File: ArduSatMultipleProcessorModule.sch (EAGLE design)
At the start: 82 parts, among them IC1 ATMEGA328P, IC2 ATMEGA328P, IC3 ATMEGA328P, IC4 ATMEGA328P, IC5 MCP23017SO, IC6 MCP23017SO, P1 N1_ICSP, P2 N0_ICSP, P3 N0_ICSP, P4 N1_ICSP, Q1 BSS138 N-MOSFET, Q2 BSS138 N-MOSFET, Q3 BSS138 N-MOSFET, Q4 BSS138 N-MOSFET, Q5 BSS138 N-MOSFET, Q6 BSS138 N-MOSFET, Q7 BSS138 N-MOSFET, Q8 BSS138 N-MOSFET, U1 MUX-74HC4067, U2 MUX-74HC4067

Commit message: Testing replacement of latches using ATmega328
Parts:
- added C13, C14: 22pF 0603, freetronics-master-v1.1:CAP0603
- added IC7: ATMEGA328P, freetronics-master-v1.1:AVR-MEGA8-MI
- added P5: N1_ICSP, freetronics-jon:ICSPSMT
- added R26: 22K 0603, freetronics-master-v1.1:RESISTOR0603
- added R32: 1M 0603, freetronics-master-v1.1:RESISTOR0603
- added R33: 33K 0603, freetronics-master-v1.1:RESISTOR0603
- added U$53: CRYSTAL-GND3X2, freetronics-jon:CRYSTAL-GND3X2
- added U3, U4: MUX-74HC4067, SparkFun:MUX-74HC4067SMD
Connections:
- removed net MGMNT_SCL: IC5.SCL, IC6.SCL, R25.1, R27.1
- removed net MGMNT_SDA: IC5.SDA, IC6.SDA, R24.1, R28.1
- removed net S0: IC5.GPA0, U1.S0, U2.S0
- removed net S1: IC5.GPA1, U1.S1, U2.S1
- removed net S2: IC5.GPA2, U1.S2, U2.S2
- removed net S3: IC5.GPA3, U1.S3, U2.S3
- new net N$22: C14.2, IC7.PB7(XTAL2/TOSC2), R32.1, U$53.XTL2
- new net N$23: C13.2, IC7.PB6(XTAL1/TOSC1), R32.2, U$53.XTL1
- new net S_A0: IC5.GPA0, IC7.PC0(ADC0), U1.S0, U2.S0, U3.S0, U4.S0
- new net S_A1: IC5.GPA1, IC7.PC1(ADC1), U1.S1, U2.S1, U3.S1, U4.S1
- new net S_A2: IC5.GPA2, IC7.PC2(ADC2), U1.S2, U2.S2, U3.S2, U4.S2
- new net S_A3: IC5.GPA3, IC7.PC3(ADC3), U1.S3, U2.S3, U3.S3, U4.S3
- new net S_A4_SDA: IC5.SDA, IC6.SDA, IC7.PC4(ADC4/SDA), R24.1, R28.1
- new net S_A5_SCL: IC5.SCL, IC6.SCL, IC7.PC5(ADC5/SCL), R25.1, R27.1
- new net S_A6: IC7.ADC6
- new net S_A7: IC7.ADC7
- new net S_D0_RX: IC7.PD0(RXD)
- new net S_D10: IC7.PB2(SS/OC1B)
- new net S_D11_MOSI: IC7.PB3(MOSI/OC2), P5.4
- new net S_D12_MISO: IC7.PB4(MISO), P5.1
- new net S_D13_SCK: IC7.PB5(SCK), P5.3
- new net S_D1_TX: IC7.PD1(TXD)
- new net S_D2: IC7.PD2(INT0)
- new net S_D3: IC7.PD3(INT1)
- new net S_D4: IC7.PD4(XCK/T0)
- new net S_D5: IC7.PD5(T1)
- new net S_D6: IC7.PD6(AIN0)
- new net S_D7: IC7.PD7(AIN1)
- new net S_D8: IC7.PB0(ICP)
- new net S_D9: IC7.PB1(OC1A)
- new net S_RESET: IC7.PC6(/RESET), P5.5, R26.1
- net +5V_SYS: now also IC7.AREF, IC7.AVCC, IC7.VCC@1, IC7.VCC@2, P5.2, R26.2, U3.VCC, U4.VCC
- net EN: now also R33.2, U3.EN, U4.EN
- net GND: now also C13.1, C14.1, IC7.AGND, IC7.GND@1, IC7.GND@2, P5.6, R33.1, U$53.GND, U$53.GND2, U3.GND, U4.GND
- net N0_D0_RX: now also U4.CHAN0
- net N0_D1_TX: now also U3.CHAN0
- net N10_D0_RX: now also U4.CHAN10
- net N10_D1_TX: now also U3.CHAN10
- net N11_D0_RX: now also U4.CHAN11
- net N11_D1_TX: now also U3.CHAN11
- net N12_D0_RX: now also U4.CHAN12
- net N12_D1_TX: now also U3.CHAN12
- net N13_D0_RX: now also U4.CHAN13
- net N13_D1_TX: now also U3.CHAN13
- net N14_D0_RX: now also U4.CHAN14
- net N14_D1_TX: now also U3.CHAN14
- net N15_D0_RX: now also U4.CHAN15
- net N15_D1_TX: now also U3.CHAN15
- net N1_D0_RX: now also U4.CHAN1
- net N1_D1_TX: now also U3.CHAN1
- net N2_D0_RX: now also U4.CHAN2
- net N2_D1_TX: now also U3.CHAN2
- net N3_D0_RX: now also U4.CHAN3
- net N3_D1_TX: now also U3.CHAN3
- net N4_D0_RX: now also U4.CHAN4
- net N4_D1_TX: now also U3.CHAN4
- net N5_D0_RX: now also U4.CHAN5
- net N5_D1_TX: now also U3.CHAN5
- net N6_D0_RX: now also U4.CHAN6
- net N6_D1_TX: now also U3.CHAN6
- net N7_D0_RX: now also U4.CHAN7
- net N7_D1_TX: now also U3.CHAN7
- net N8_D0_RX: now also U4.CHAN8
- net N8_D1_TX: now also U3.CHAN8
- net N9_D0_RX: now also U4.CHAN9
- net N9_D1_TX: now also U3.CHAN9
- net RX: now also U4.COM
- net TX: now also U3.COM
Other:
- note added: "Supervisor"

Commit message: Added alternative supervisor node
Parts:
- added JP3: (no value), freetronics-master-v1.1:M02PTH
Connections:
- net RX: now also JP3.2
- net TX: now also JP3.1
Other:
- note added: "ATmega328P core consumes ~10mA at 5V / 16MHz"
- note added: "May not be suitable for direct control of node VCCs."
- note removed: "Not suitable for direct control of node VCCs."
- moved on the sheet: C1, C10, C11, C12, C13, C14, C2, C3, C4, C5, C6, C7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

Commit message: Added VCC control for nodes 0 and 1
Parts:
- removed C12: 100nF 0603, freetronics-master-v1.1:CAP0603
- added C15: 100nF 0603, freetronics-master-v1.1:CAP0603
- added Q10, Q9: 2N7002 N-MOSFET, freetronics-master-v1:MOSFET-NCHANNELSMD
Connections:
- net EN renamed UART_EN
- net S_D0_RX renamed S_D0_N2_PWR
- net S_D1_TX renamed S_D1_N3_PWR
- net S_D2 renamed S_D2_N4_PWR
- net S_D3 renamed S_D3_N5_PWR
- net S_D4 renamed S_D4_N6_PWR
- removed net S_A6: IC7.ADC6
- removed net S_A7: IC7.ADC7
- new net S_A6_N0_PWR: IC7.ADC6, Q9.G
- new net S_A7_N1_PWR: IC7.ADC7, Q10.G
- net +5V_SYS: now also Q10.S, Q9.S
- net GND: now also C15.2; no longer C12.2
- net N0_5V: now also Q9.D
- net N1_5V: now also C15.1, Q10.D; no longer C12.1
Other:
- note added: "Add FETs or something to switch node VCCs?"
- note added: "Add watchdog (voltage + heartbeat?) to supervisor"
- note added: "Control UART switch EN from supervisor"
- note added: "Node 0"
- note added: "Node 1"
- note added: "Power Control"
- note added: "Processor"
- note removed: "Add FETs or something to switch node VCCs"
- note removed: "Processor Node 0"
- note removed: "Processor Node 1"
- moved on the sheet: C10, C11, C7, C8, C9, IC3, IC4, P3, P4, Q5, Q6, Q7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

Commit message: Supervisor now has control of both node power and serial comms
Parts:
- removed U1, U2, U3, U4: MUX-74HC4067, SparkFun:MUX-74HC4067SMD
- added IC8: MCP23S17ML, freetronics-jon:MCP23S17ML
- added U$57, U$58, U$59, U$60: MUX-74HC4067-QFNSMT, freetronics-jon:MUX-74HC4067-QFNSMT
- IC5, IC6: value MCP23017SO -> MCP23017ML; device microchip:MCP23017SO -> freetronics-jon:MCP23017ML
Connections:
- net S_D0_N2_PWR renamed S_D0
- net S_D1_N3_PWR renamed S_D1
- net S_D2_N4_PWR renamed S_D2
- net S_D3_N5_PWR renamed S_D3
- net S_D4_N6_PWR renamed S_D4
- removed net N10_5V: IC6.GPB2
- removed net N11_5V: IC6.GPB3
- removed net N12_5V: IC6.GPB4
- removed net N13_5V: IC6.GPB5
- removed net N14_5V: IC6.GPB6
- removed net N15_5V: IC6.GPB7
- removed net N4_5V: IC6.GPA4
- removed net N5_5V: IC6.GPA5
- removed net N6_5V: IC6.GPA6
- removed net N7_5V: IC6.GPA7
- removed net N8_5V: IC6.GPB0
- removed net N9_5V: IC6.GPB1
- removed net S_A6_N0_PWR: IC7.ADC6, Q9.G
- removed net S_A7_N1_PWR: IC7.ADC7, Q10.G
- new net N$90: IC8.!RESET
- new net N0_PWR: IC6.GPA0, IC8.GPA0, Q9.G
- new net N10_PWR: IC6.GPB2, IC8.GPB2
- new net N11_PWR: IC6.GPB3, IC8.GPB3
- new net N12_PWR: IC6.GPB4, IC8.GPB4
- new net N13_PWR: IC6.GPB5, IC8.GPB5
- new net N14_PWR: IC6.GPB6, IC8.GPB6
- new net N15_PWR: IC6.GPB7, IC8.GPB7
- new net N1_PWR: IC6.GPA1, IC8.GPA1, Q10.G
- new net N2_PWR: IC6.GPA2, IC8.GPA2
- new net N3_PWR: IC6.GPA3, IC8.GPA3
- new net N4_PWR: IC6.GPA4, IC8.GPA4
- new net N5_PWR: IC6.GPA5, IC8.GPA5
- new net N6_PWR: IC6.GPA6, IC8.GPA6
- new net N7_PWR: IC6.GPA7, IC8.GPA7
- new net N8_PWR: IC6.GPB0, IC8.GPB0
- new net N9_PWR: IC6.GPB1, IC8.GPB1
- new net S_A6: IC7.ADC6, R33.1, U$59.EN, U$60.EN
- new net S_A7: IC7.ADC7
- net +5V_SYS: now also IC8.VDD, R33.2, U$57.VCC, U$57.VCC1, U$58.VCC, U$58.VCC1, U$59.VCC, U$59.VCC1, U$60.VCC, U$60.VCC1; no longer U1.VCC, U2.VCC, U3.VCC, U4.VCC
- net GND: now also IC8.A0, IC8.A1, IC8.A2, IC8.VSS, U$57.GND, U$58.GND, U$59.GND, U$60.GND; no longer R33.1, U1.GND, U2.GND, U3.GND, U4.GND
- net N0_5V: no longer IC6.GPA0
- net N0_D0_RX: now also U$58.Y0, U$59.Y0; no longer U2.CHAN0, U4.CHAN0
- net N0_D1_TX: now also U$57.Y0, U$60.Y0; no longer U1.CHAN0, U3.CHAN0
- net N10_D0_RX: now also U$58.Y10, U$59.Y10; no longer U2.CHAN10, U4.CHAN10
- net N10_D1_TX: now also U$57.Y10, U$60.Y10; no longer U1.CHAN10, U3.CHAN10
- net N11_D0_RX: now also U$58.Y11, U$59.Y11; no longer U2.CHAN11, U4.CHAN11
- net N11_D1_TX: now also U$57.Y11, U$60.Y11; no longer U1.CHAN11, U3.CHAN11
- net N12_D0_RX: now also U$58.Y12, U$59.Y12; no longer U2.CHAN12, U4.CHAN12
- net N12_D1_TX: now also U$57.Y12, U$60.Y12; no longer U1.CHAN12, U3.CHAN12
- net N13_D0_RX: now also U$58.Y13, U$59.Y13; no longer U2.CHAN13, U4.CHAN13
- net N13_D1_TX: now also U$57.Y13, U$60.Y13; no longer U1.CHAN13, U3.CHAN13
- net N14_D0_RX: now also U$58.Y14, U$59.Y14; no longer U2.CHAN14, U4.CHAN14
- net N14_D1_TX: now also U$57.Y14, U$60.Y14; no longer U1.CHAN14, U3.CHAN14
- net N15_D0_RX: now also U$58.Y15, U$59.Y15; no longer U2.CHAN15, U4.CHAN15
- net N15_D1_TX: now also U$57.Y15, U$60.Y15; no longer U1.CHAN15, U3.CHAN15
- net N1_5V: no longer IC6.GPA1
- net N1_D0_RX: now also U$58.Y1, U$59.Y1; no longer U2.CHAN1, U4.CHAN1
- net N1_D1_TX: now also U$57.Y1, U$60.Y1; no longer U1.CHAN1, U3.CHAN1
- net N2_5V: no longer IC6.GPA2
- net N2_D0_RX: now also U$58.Y2, U$59.Y2; no longer U2.CHAN2, U4.CHAN2
- net N2_D1_TX: now also U$57.Y2, U$60.Y2; no longer U1.CHAN2, U3.CHAN2
- net N3_5V: no longer IC6.GPA3
- net N3_D0_RX: now also U$58.Y3, U$59.Y3; no longer U2.CHAN3, U4.CHAN3
- net N3_D1_TX: now also U$57.Y3, U$60.Y3; no longer U1.CHAN3, U3.CHAN3
- net N4_D0_RX: now also U$58.Y4, U$59.Y4; no longer U2.CHAN4, U4.CHAN4
- net N4_D1_TX: now also U$57.Y4, U$60.Y4; no longer U1.CHAN4, U3.CHAN4
- net N5_D0_RX: now also U$58.Y5, U$59.Y5; no longer U2.CHAN5, U4.CHAN5
- net N5_D1_TX: now also U$57.Y5, U$60.Y5; no longer U1.CHAN5, U3.CHAN5
- net N6_D0_RX: now also U$58.Y6, U$59.Y6; no longer U2.CHAN6, U4.CHAN6
- net N6_D1_TX: now also U$57.Y6, U$60.Y6; no longer U1.CHAN6, U3.CHAN6
- net N7_D0_RX: now also U$58.Y7, U$59.Y7; no longer U2.CHAN7, U4.CHAN7
- net N7_D1_TX: now also U$57.Y7, U$60.Y7; no longer U1.CHAN7, U3.CHAN7
- net N8_D0_RX: now also U$58.Y8, U$59.Y8; no longer U2.CHAN8, U4.CHAN8
- net N8_D1_TX: now also U$57.Y8, U$60.Y8; no longer U1.CHAN8, U3.CHAN8
- net N9_D0_RX: now also U$58.Y9, U$59.Y9; no longer U2.CHAN9, U4.CHAN9
- net N9_D1_TX: now also U$57.Y9, U$60.Y9; no longer U1.CHAN9, U3.CHAN9
- net RX: now also U$58.Z, U$59.Z; no longer U2.COM, U4.COM
- net S_A0: now also U$57.S0, U$58.S0, U$59.S0, U$60.S0; no longer U1.S0, U2.S0, U3.S0, U4.S0
- net S_A1: now also U$57.S1, U$58.S1, U$59.S1, U$60.S1; no longer U1.S1, U2.S1, U3.S1, U4.S1
- net S_A2: now also U$57.S2, U$58.S2, U$59.S2, U$60.S2; no longer U1.S2, U2.S2, U3.S2, U4.S2
- net S_A3: now also U$57.S3, U$58.S3, U$59.S3, U$60.S3; no longer U1.S3, U2.S3, U3.S3, U4.S3
- net S_D10: now also IC8.!CS
- net S_D11_MOSI: now also IC8.SI
- net S_D12_MISO: now also IC8.SO
- net S_D13_SCK: now also IC8.SCK
- net TX: now also U$57.Z, U$60.Z; no longer U1.COM, U3.COM
- net UART_EN: now also U$57.EN, U$58.EN; no longer R33.2, U1.EN, U2.EN, U3.EN, U4.EN
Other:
- note added: "Pass through RESET for each node? Easy, but better perhaps to expose one of the Supervisor node I/O lines as a "virtual" reset line, which in turn toggles power to that node. That way the interface to this board externally just looks like TX, RX, and RESET, like any other Arduino. It would just need the node selected first"
- note added: "http://arduino.cc/playground/Main/MCP23S17"
- moved on the sheet: C13, C14, IC6, IC7, JP1, JP2, JP3, LED4, P5, R10, R20, R22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

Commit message: Removed direct control option for UART MUX and power
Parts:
- removed IC5, IC6: MCP23017ML, freetronics-jon:MCP23017ML
- removed JP7: (no value), freetronics-master-v1.1:PINHD-2X3
- removed R24, R25, R27, R28: 4K7, freetronics-master-v1:RESISTOR0603
- removed R29, R30, R31: 33K, freetronics-master-v1:RESISTOR0603
- removed U$57, U$58: MUX-74HC4067-QFNSMT, freetronics-jon:MUX-74HC4067-QFNSMT
- added Q11, Q12: BSS138 N-MOSFET, freetronics-master-v1:MOSFET-NCHANNELSMD
- JP2: device freetronics-master-v1.1:PINHD-2X3 -> freetronics-master-v1.1:M02PTH
- R20: value 33K -> 100K 0603; device freetronics-master-v1:RESISTOR0603 -> freetronics-master-v1.1:RESISTOR0603
- R21: value 33K 0603 -> 100K 0603
- R22, R23: value 33K -> 10K 0603; device freetronics-master-v1:RESISTOR0603 -> freetronics-master-v1.1:RESISTOR0603
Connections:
- removed net ADDR0: IC5.A0, JP7.2, R29.2
- removed net ADDR1: IC5.A1, JP7.4, R30.2
- removed net ADDR2: IC5.A2, JP7.6, R31.2
- removed net PWR_ADDR0: IC6.A0, JP2.2, R20.2
- removed net PWR_ADDR1: IC6.A1, JP2.4, R22.2
- removed net PWR_ADDR2: IC6.A2, JP2.6, R23.2
- removed net RESET: IC5.!RESET, IC6.!RESET
- removed net SCL: JP1.2, Q2.D, Q4.D, Q6.D, Q8.D, R5.1
- removed net SDA: JP1.1, Q1.D, Q3.D, Q5.D, Q7.D, R4.1
- removed net UART_EN: R21.2, U$57.EN, U$58.EN
- new net MGMNT_SCL: JP1.2, Q12.D, R5.1
- new net MGMNT_SDA: JP1.1, Q11.D, R4.1
- new net NODE_SCL: JP2.2, Q2.D, Q4.D, Q6.D, Q8.D, R21.1
- new net NODE_SDA: JP2.1, Q1.D, Q3.D, Q5.D, Q7.D, R20.1
- net +5V_SYS: now also R20.2, R21.2; no longer IC5.VDD, IC6.VDD, JP2.1, JP2.3, JP2.5, JP7.1, JP7.3, JP7.5, R24.2, R25.2, R27.2, R28.2, U$57.VCC, U$57.VCC1, U$58.VCC, U$58.VCC1
- net GND: no longer IC5.VSS, IC6.VSS, R20.1, R21.1, R22.1, R23.1, R29.1, R30.1, R31.1, U$57.GND, U$58.GND
- net N0_D0_RX: no longer U$58.Y0
- net N0_D1_TX: no longer U$57.Y0
- net N0_PWR: no longer IC6.GPA0
- net N10_D0_RX: no longer U$58.Y10
- net N10_D1_TX: no longer U$57.Y10
- net N10_PWR: no longer IC6.GPB2
- net N11_D0_RX: no longer U$58.Y11
- net N11_D1_TX: no longer U$57.Y11
- net N11_PWR: no longer IC6.GPB3
- net N12_D0_RX: no longer U$58.Y12
- net N12_D1_TX: no longer U$57.Y12
- net N12_PWR: no longer IC6.GPB4
- net N13_D0_RX: no longer U$58.Y13
- net N13_D1_TX: no longer U$57.Y13
- net N13_PWR: no longer IC6.GPB5
- net N14_D0_RX: no longer U$58.Y14
- net N14_D1_TX: no longer U$57.Y14
- net N14_PWR: no longer IC6.GPB6
- net N15_D0_RX: no longer U$58.Y15
- net N15_D1_TX: no longer U$57.Y15
- net N15_PWR: no longer IC6.GPB7
- net N1_5V: now also Q11.G, Q12.G, R22.2, R23.2
- net N1_D0_RX: no longer U$58.Y1
- net N1_D1_TX: no longer U$57.Y1
- net N1_PWR: no longer IC6.GPA1
- net N2_D0_RX: no longer U$58.Y2
- net N2_D1_TX: no longer U$57.Y2
- net N2_PWR: no longer IC6.GPA2
- net N3_D0_RX: no longer U$58.Y3
- net N3_D1_TX: no longer U$57.Y3
- net N3_PWR: no longer IC6.GPA3
- net N4_D0_RX: no longer U$58.Y4
- net N4_D1_TX: no longer U$57.Y4
- net N4_PWR: no longer IC6.GPA4
- net N5_D0_RX: no longer U$58.Y5
- net N5_D1_TX: no longer U$57.Y5
- net N5_PWR: no longer IC6.GPA5
- net N6_D0_RX: no longer U$58.Y6
- net N6_D1_TX: no longer U$57.Y6
- net N6_PWR: no longer IC6.GPA6
- net N7_D0_RX: no longer U$58.Y7
- net N7_D1_TX: no longer U$57.Y7
- net N7_PWR: no longer IC6.GPA7
- net N8_D0_RX: no longer U$58.Y8
- net N8_D1_TX: no longer U$57.Y8
- net N8_PWR: no longer IC6.GPB0
- net N9_D0_RX: no longer U$58.Y9
- net N9_D1_TX: no longer U$57.Y9
- net N9_PWR: no longer IC6.GPB1
- net RX: no longer U$58.Z
- net S_A0: no longer IC5.GPA0, U$57.S0, U$58.S0
- net S_A1: no longer IC5.GPA1, U$57.S1, U$58.S1
- net S_A2: no longer IC5.GPA2, U$57.S2, U$58.S2
- net S_A3: no longer IC5.GPA3, U$57.S3, U$58.S3
- net S_A4_SDA: now also Q11.S, R22.1; no longer IC5.SDA, IC6.SDA, R24.1, R28.1
- net S_A5_SCL: now also Q12.S, R23.1; no longer IC5.SCL, IC6.SCL, R25.1, R27.1
- net TX: no longer U$57.Z
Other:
- note added: "Add status LEDs to the MUX address and enable lines?"
- note added: "I2C Bias: Management Bus"
- note added: "I2C Bias: Node Bus"
- note removed: "1"
- note removed: "2"
- note removed: "4"
- note removed: "I2C Bias"
- moved on the sheet: JP1, JP3, LED4, R10, R20, R21, R22, R23, R4, R5

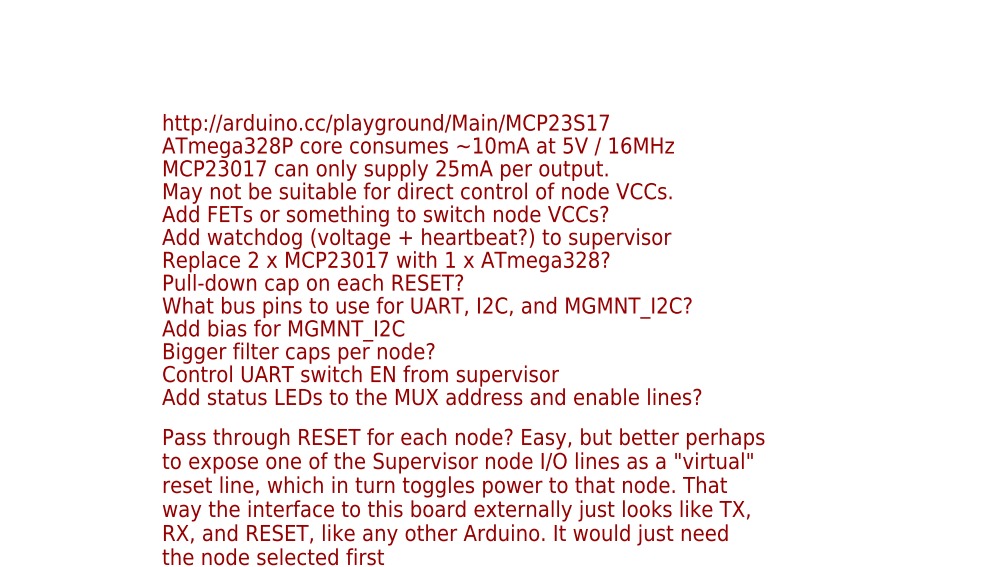
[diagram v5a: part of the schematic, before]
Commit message: Experiments with node layout
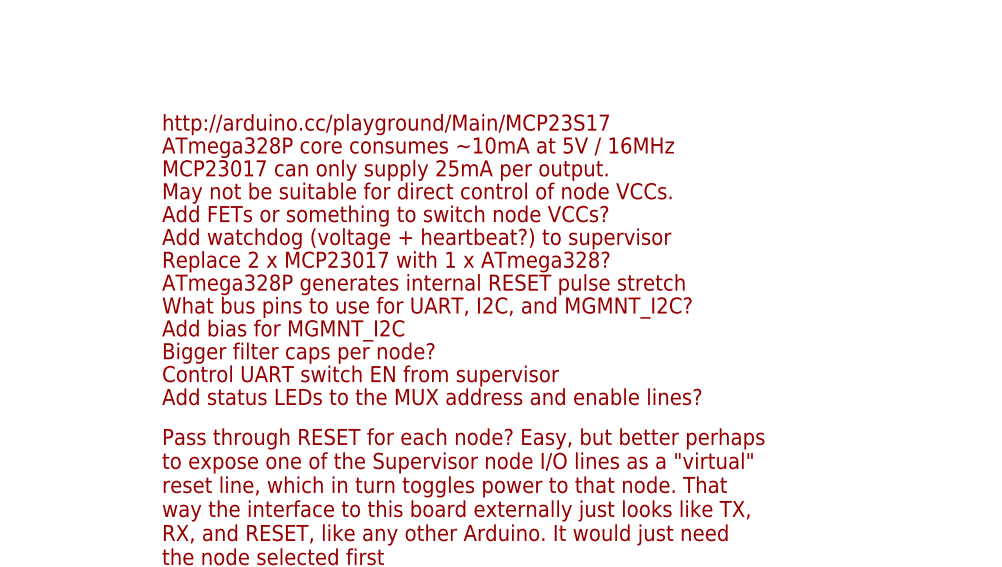
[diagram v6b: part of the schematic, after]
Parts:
- P3: device freetronics-jon:ICSPSMT -> freetronics-jon:ICSPPTH
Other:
- note added: "ATmega328P generates internal RESET pulse stretch"
- note removed: "Pull-down cap on each RESET?"
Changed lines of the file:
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@@
 <part name="R12" library="freetronics-master-v1.1" deviceset="RESISTOR" device="0603" value="22K 0603"/>
 <part name="U$26" library="SparkFun" deviceset="5V" device=""/>
-<part name="P3" library="freetronics-jon" deviceset="ICSP" device="SMT" value="N0_ICSP"/>
+<part name="P3" library="freetronics-jon" deviceset="ICSP" device="PTH" value="N0_ICSP"/>
 <part name="GND14" library="SparkFun" deviceset="GND" device=""/>
 <part name="U$27" library="SparkFun" deviceset="5V" device=""/>
@@
 <text x="99.06" y="63.5" size="1.778" layer="94">Add bias for MGMNT_I2C</text>
 <text x="99.06" y="60.96" size="1.778" layer="94">Bigger filter caps per node?</text>
-<text x="99.06" y="68.58" size="1.778" layer="94">Pull-down cap on each RESET?</text>
+<text x="99.06" y="68.58" size="1.778" layer="94">ATmega328P generates internal RESET pulse stretch</text>
 <text x="264.16" y="177.038" size="1.778" layer="94" distance="58">Supervisor</text>
 <frame x1="254" y1="0" x2="502.92" y2="185.42" columns="8" rows="5" layer="94"/>
